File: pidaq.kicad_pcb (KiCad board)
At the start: 2 copper layers, 95.2 x 95.3 mm, 46 parts, among them J1 Screw_Terminal_01x10, J2 Screw_Terminal_01x10, J3 Screw_Terminal_01x08, J4 Screw_Terminal_01x08, J5 Conn_01x03_Male, J6 Conn_01x08_Female, J7 Screw_Terminal_01x04, J8 Conn_01x03_Male, U1 LTC2984CLX-DNP, U2 LTC2449CUHF, U3 SN74LV1T34DCKR, U4 INA126U

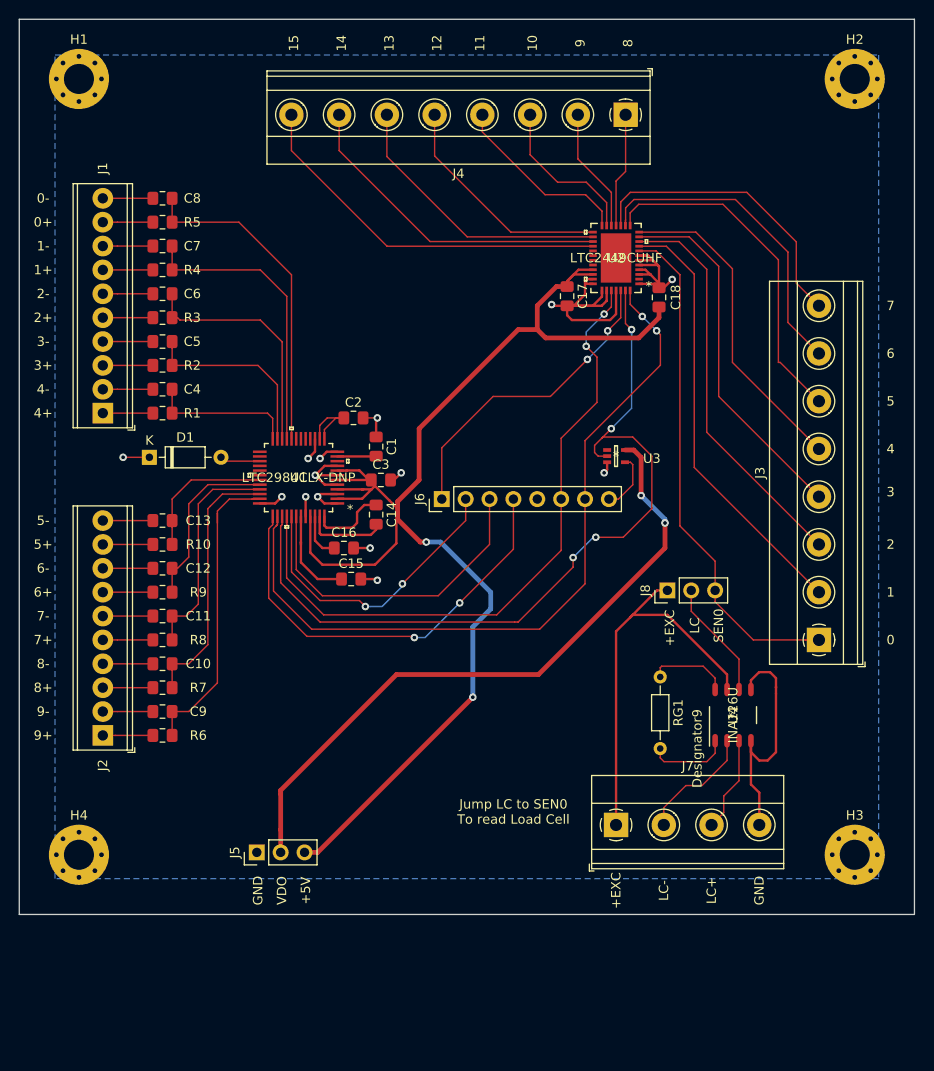
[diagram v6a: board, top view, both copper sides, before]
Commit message: added low pass filter to load cell inputs
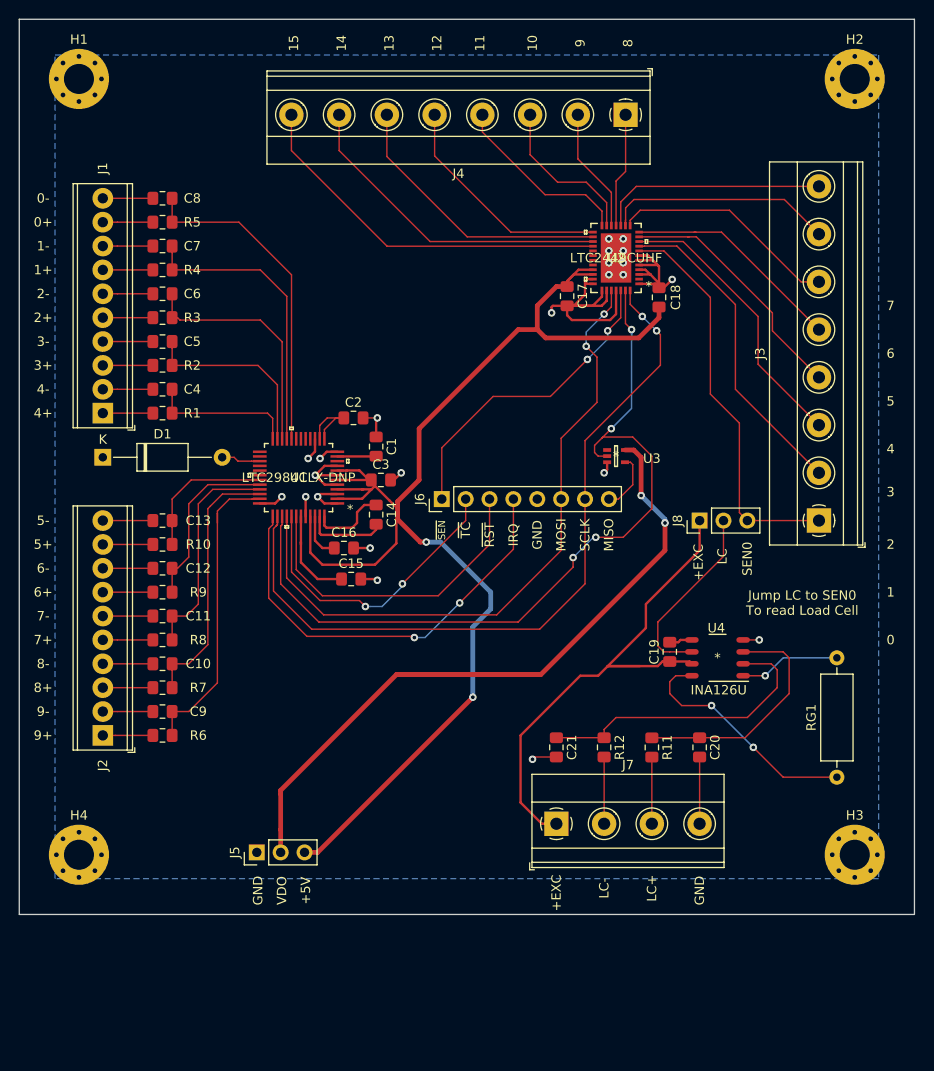
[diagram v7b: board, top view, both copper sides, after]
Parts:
- added C19: 0.1uF, Capacitor_SMD:C_0805_2012Metric_Pad1.15x1.40mm_HandSolder, F.Cu at (139.1, 118.1)
- added C20: C, Capacitor_SMD:C_0805_2012Metric_Pad1.15x1.40mm_HandSolder, F.Cu at (142.2, 128.3)
- added C21: C, Capacitor_SMD:C_0805_2012Metric_Pad1.15x1.40mm_HandSolder, F.Cu at (127.0, 128.3)
- added R11: R_US, Resistor_SMD:R_0805_2012Metric_Pad1.15x1.40mm_HandSolder, F.Cu at (137.2, 128.3)
- added R12: R_US, Resistor_SMD:R_0805_2012Metric_Pad1.15x1.40mm_HandSolder, F.Cu at (132.1, 128.3)
- D1: footprint Diode_THT:D_DO-35_SOD27_P7.62mm_Horizontal -> Diode_THT:D_A-405_P12.70mm_Horizontal
- RG1: footprint Resistor_THT:R_Axial_DIN0204_L3.6mm_D1.6mm_P7.62mm_Horizontal -> Resistor_THT:R_Axial_DIN0309_L9.0mm_D3.2mm_P12.70mm_Horizontal
- moved RG1 21.6 mm to (156.8, 131.4), turned to 90 degrees
- moved J3 12.7 mm to (154.9, 104.1)
- moved J8 8.18 mm to (142.2, 104.1)
- moved J7 6.35 mm to (127.0, 136.4)
- moved U4 6.32 mm to (144.1, 118.7), turned to 180 degrees
- moved D1 4.95 mm to (78.7, 97.4)
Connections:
- U4 pad 2: LC- -> /sensors/LC-_Filter
- U4 pad 3: LC+ -> /sensors/LC+_Filter
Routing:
- net /sensors/LC-_Filter: track 0.00 -> 32.0 mm
- net /sensors/LC+_Filter: track 0.00 -> 25.5 mm
- net Net-(RG1-Pad1): track 8.63 -> 25.4 mm, vias 0 -> 2
- net VDOUT: track 70.9 -> 86.2 mm
- net GND: track 156.9 -> 142.5 mm, vias 14 -> 23
- net +EXC: track 42.6 -> 56.4 mm
- net SEN0: track 55.9 -> 42.6 mm
- net SEN5: track 36.9 -> 24.2 mm
- net SEN2: track 42.6 -> 30.2 mm
- net SEN3: track 38.7 -> 26.6 mm
- net SEN1: track 46.4 -> 34.4 mm
- net SEN4: track 34.5 -> 23.6 mm
- net SEN6: track 34.0 -> 24.4 mm
- net LC: track 12.7 -> 20.1 mm
- net SEN7: track 31.6 -> 24.3 mm
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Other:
- board text added: "IRQ"
- board text added: "MISO"
- board text added: "MOSI"
- board text added: "SCLK"
- board text added: "~RST"
- board text added: "~SEN"
- board text added: "~TC"

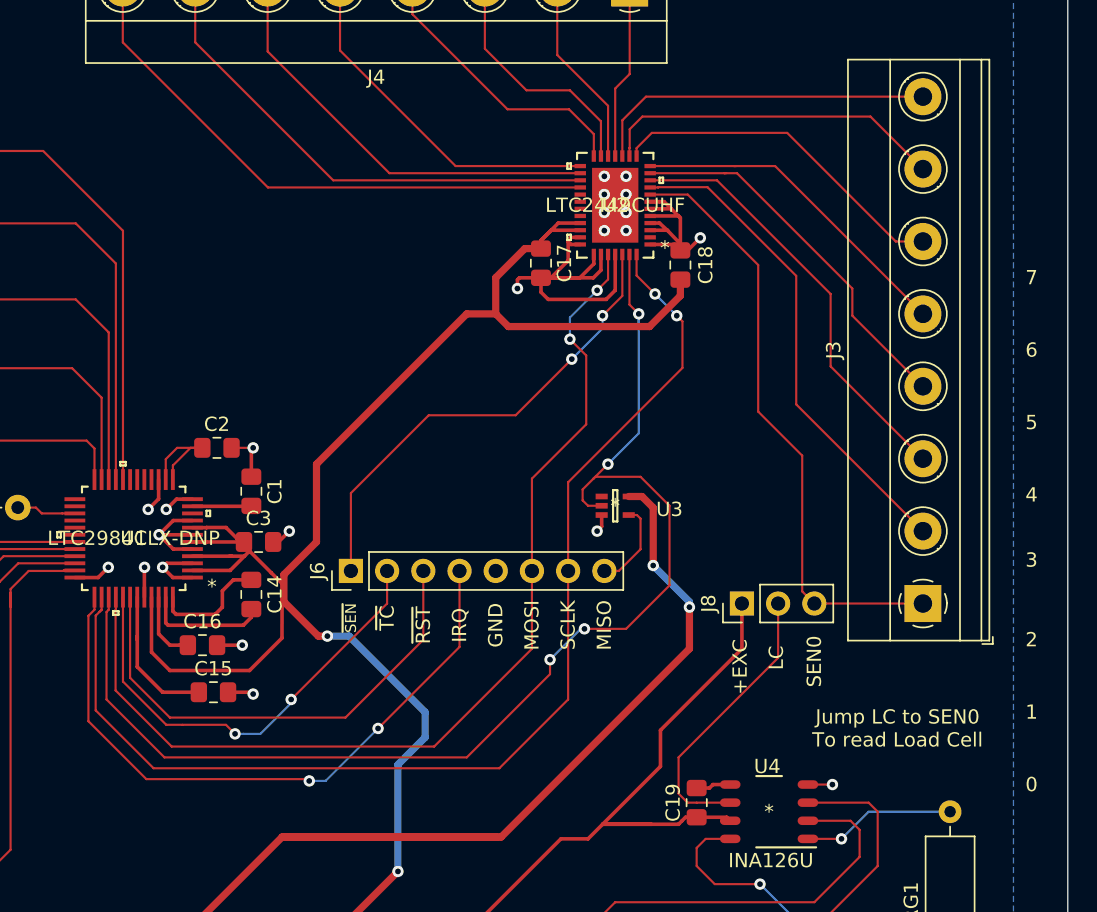
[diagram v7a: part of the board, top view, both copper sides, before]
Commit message: touched up silkscreen and trace spacing
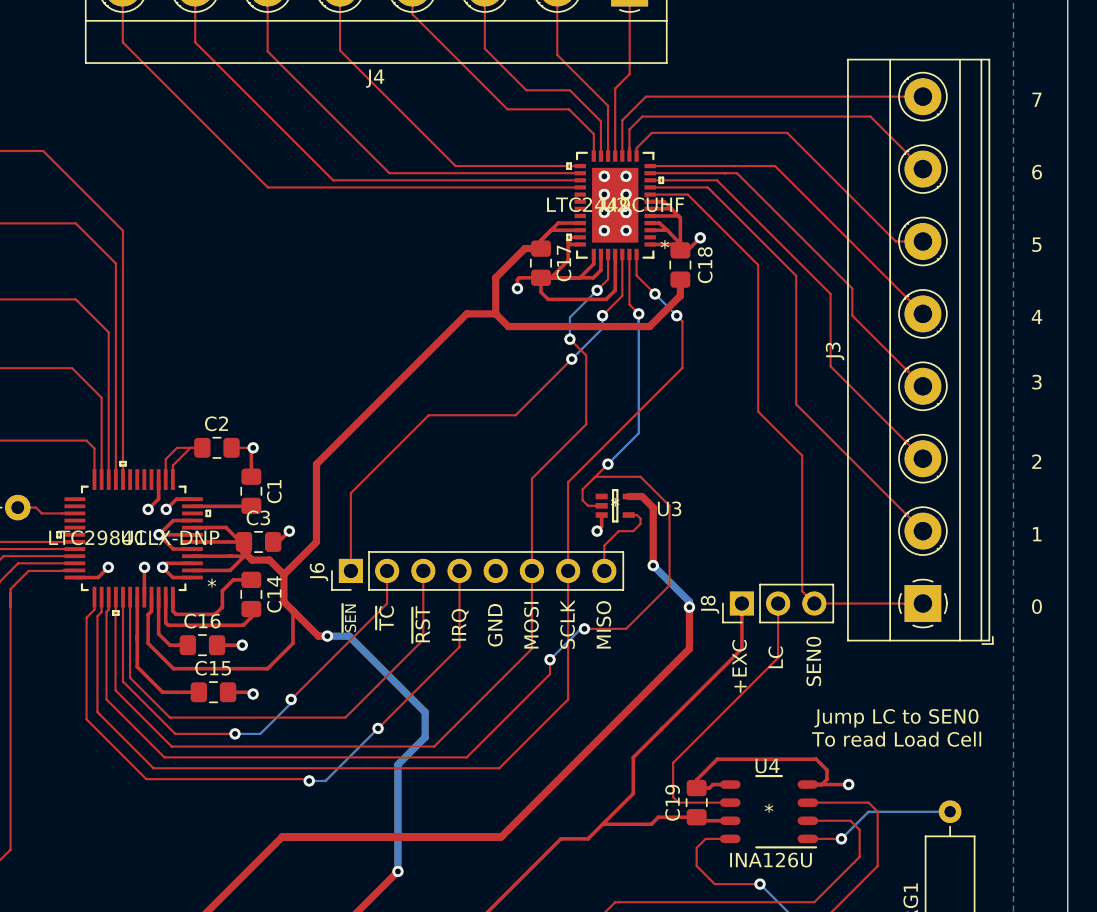
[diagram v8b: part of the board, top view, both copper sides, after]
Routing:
- net GND: track 142.5 -> 156.4 mm
- net +EXC: track 56.4 -> 53.2 mm
- net LC: track 20.1 -> 20.8 mm
